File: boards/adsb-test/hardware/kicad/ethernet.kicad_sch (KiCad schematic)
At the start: 0 parts

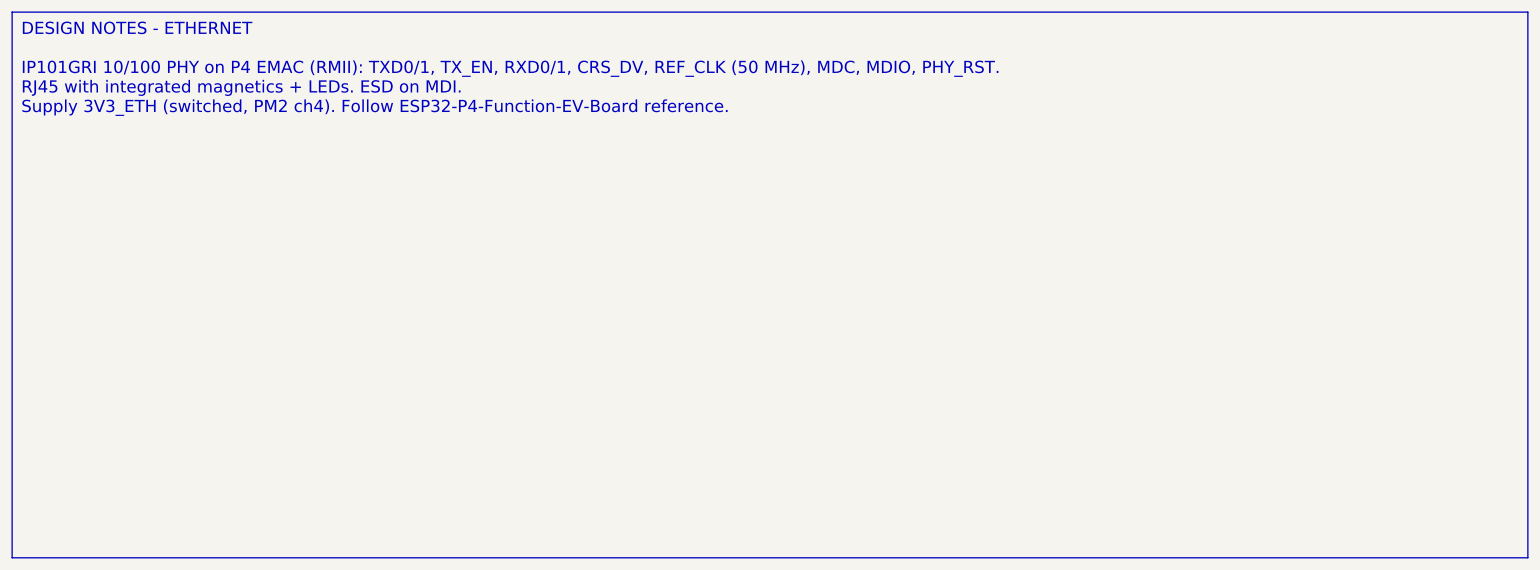
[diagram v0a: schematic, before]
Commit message: Release v0.4.0: ADSB_Test with ESP32-C5, ADSBee m1421 and LA5016 header
- C6 -> C5 co-processor; m1421 identified and integrated (symbol/footprint
  from the ADSBee 1421 carrier, GPL-3.0 attribution)
- Power budget and 2S1P battery sizing for >= 1 h; USB-A for 1-2 SDRs via hub
- Dev port: FT2232H + RP2040 debugprobe; TCA6408A expander for slow I/O
- Test Debug sheet with LA5016 header and rail test points
- Vendor documents git-ignored (public repo)

Co-Authored-By: Claude Opus 5.5 <noreply@anthropic.com>
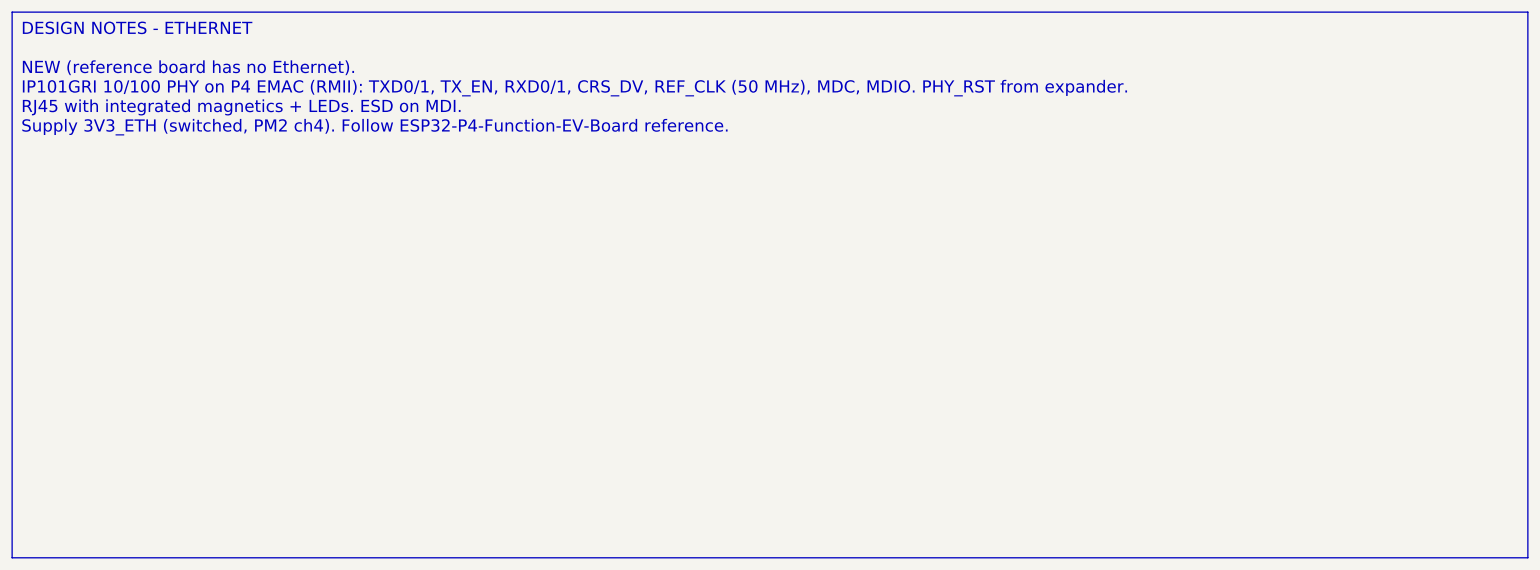
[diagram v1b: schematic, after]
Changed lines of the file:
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@@
 		(comment 1 "Requirements: boards/adsb-test/docs/requirements.md")
 	)
-	(text_box "DESIGN NOTES - ETHERNET\n\nIP101GRI 10/100 PHY on P4 EMAC (RMII): TXD0/1, TX_EN, RXD0/1, CRS_DV, REF_CLK (50 MHz), MDC, MDIO, PHY_RST.\nRJ45 with integrated magnetics + LEDs. ESD on MDI.\nSupply 3V3_ETH (switched, PM2 ch4). Follow ESP32-P4-Function-EV-Board reference."
+	(text_box "DESIGN NOTES - ETHERNET\n\nNEW (reference board has no Ethernet).\nIP101GRI 10/100 PHY on P4 EMAC (RMII): TXD0/1, TX_EN, RXD0/1, CRS_DV, REF_CLK (50 MHz), MDC, MDIO. PHY_RST from expander.\nRJ45 with integrated magnetics + LEDs. ESD on MDI.\nSupply 3V3_ETH (switched, PM2 ch4). Follow ESP32-P4-Function-EV-Board reference."
 		(exclude_from_sim no)
 		(at 20 20 0)
